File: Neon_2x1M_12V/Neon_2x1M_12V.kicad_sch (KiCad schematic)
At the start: 48 parts, among them J1 Conn_01x16_Pin, J2 Barrel_Jack_MountingPin, J3 Conn_01x16_Pin, J4 Barrel_Jack_MountingPin, J5 Barrel_Jack_MountingPin, J6 Conn_01x03_Pin, Q1 IRLML2502TRPBF, Q2 IRLML2502TRPBF, Q3 BSS138, Q4 BSS138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

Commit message: update BOM only 1k resistor is needed
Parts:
- Q3, Q4, Q5: value BSS138 -> Si2302DS; link https://makerselectronics.com/product/smd-mosfet-transistor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 -> https://uge-one.com/product/si2302ds-sot23-general-purpose-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
- R1: value 2.2k Ohm -> 1k Ohm
- R13: value 660 Ohm -> 680 Ohm
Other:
- note added: "BLUE LED, Vf=3V: V accross resistor = 3.3 - 3 = 0.3V I = V/R = 0.3/1000 = 0.3mAmp"
- note added: "for each LED (color): R = (Vsource - Vf) / I_Led p_R = (Vsource - Vf) * I_Led Red (Vf = 2.1 V) V_r = 12 − 2.1 = 9.9 V R = 9.9 / 0.015 = 660 Ω use standard 680 Ω I = 9.9 / 680 Ω = 14.5 mAmp P_R = 9.9 * 0.0145 = 0.14355 W (1/4 W resistor fine) Green (Vf = 2.8 V) V_r = 12 − 2.8 = 9.2 V R = 9.2 / 0.015 = 613.33 Ω use standard 600Ω I = 9.2 / 600 Ω = 15.3 mAmp P_R = 9.2 * 0.0153 = 0.14076 W Blue (Vf = 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"
- note removed: "BLUE LED, Vf=3V: V accross resistor = 3.3 - 3 = 0.3V I = V/R = 0.3/2200 = 0.59mAmp"
- note removed: "for each LED (color): R = (Vsource - Vf) / I_Led p_R = (Vsource - Vf) * I_Led Per LED current = 12 mA / 3 LEDs = 4.0 mA each. Red (Vf = 2.1 V) V_r = 12 − 2.1 = 9.9 V R = 9.9 / 0.015 = 660 Ω use standard 680 Ω I = 9.9 / 680 Ω = 14.5 mAmp P_R = 9.9 * 0.0145 = 0.14355 W (1/4 W resistor fine) Green (Vf = 2.8 V) V_r = 12 − 2.8 = 9.2 V R = 9.2 / 0.015 = 613.33 Ω use standard 600Ω I = 9.2 / 600 Ω = 15.3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"
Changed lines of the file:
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@@
 		)
 	)
-	(text "for each LED (color):\nR = (Vsource - Vf) / I_Led\np_R = (Vsource - Vf) * I_Led\n\nPer LED current = 12 mA / 3 LEDs = 4.0 mA each.\n\nRed (Vf = 2.1 V)\nV_r = 12 − 2.1 = 9.9 V\nR = 9.9 / 0.015 = 660 Ω \nuse standard 680 Ω\nI = 9.9 / 680 Ω = 14.5 mAmp\nP_R = 9.9 * 0.0145 = 0.14355 W (1/4 W resistor fine)\n\nGreen (Vf = 2.8 V)\nV_r = 12 − 2.8 = 9.2 V\nR = 9.2 / 0.015 = 613.33 Ω \nuse standard  600Ω\nI = 9.2 / 600 Ω = 15.3 mAmp\nP_R = 9.2 * 0.0153 = 0.14076 W\n\nBlue (Vf = 3.2 V)\nsame as green "
+	(text "for each LED (color):\nR = (Vsource - Vf) / I_Led\np_R = (Vsource - Vf) * I_Led\n\nRed (Vf = 2.1 V)\nV_r = 12 − 2.1 = 9.9 V\nR = 9.9 / 0.015 = 660 Ω \nuse standard 680 Ω\nI = 9.9 / 680 Ω = 14.5 mAmp\nP_R = 9.9 * 0.0145 = 0.14355 W (1/4 W resistor fine)\n\nGreen (Vf = 2.8 V)\nV_r = 12 − 2.8 = 9.2 V\nR = 9.2 / 0.015 = 613.33 Ω \nuse standard  600Ω\nI = 9.2 / 600 Ω = 15.3 mAmp\nP_R = 9.2 * 0.0153 = 0.14076 W\n\nBlue (Vf = 2.8 V)\nsame as green "
 		(exclude_from_sim no)
 		(at 96.012 156.464 0)
@@
 		)
 	)
-	(text "BLUE LED, Vf=3V:\nV accross resistor = 3.3 - 3 = 0.3V\nI = V/R = 0.3/2200 = 0.59mAmp"
+	(text "BLUE LED, Vf=3V:\nV accross resistor = 3.3 - 3 = 0.3V\nI = V/R = 0.3/1000 = 0.3mAmp"
 		(exclude_from_sim no)
 		(at 185.928 105.664 0)
@@
 			)
 		)
-		(property "Value" "660 Ohm"
+		(property "Value" "680 Ohm"
 			(at 142.24 82.55 90)
 			(effects
@@
 			)
 		)
-		(property "Value" "BSS138"
+		(property "Value" "Si2302DS"
 			(at 114.808 119.634 0)
 			(effects
@@
 			)
 		)
-		(property "Datasheet" "https://www.onsemi.com/pub/Collateral/BSS138-D.PDF"
+		(property "Datasheet" "https://www.vishay.com/docs/68645/si2302cds.pdf"
 			(at 114.3 121.92 0)
 			(effects
@@
 			)
 		)
-		(property "Description" "50V Vds, 0.22A Id, N-Channel MOSFET, SOT-23"
+		(property "Description" ""
 			(at 109.22 118.11 0)
 			(effects
@@
 			)
 		)
-		(property "link" "https://makerselectronics.com/product/smd-mosfet-transistor-bss138-j1-50v-220ma-3-5%CF%8910v220ma-360mw-n-channel-sot-23/?srsltid=AfmBOorKPkIxsAwv-3Onwyym6kfiJ7AE8Pv9g0Pld8GAUTAgILHxbmr_"
+		(property "link" "https://uge-one.com/product/si2302ds-sot23-general-purpose-n-channel-mosfet-smd-transistor-sot-23/"
 			(at 109.22 118.11 0)
 			(effects
@@
 			)
 		)
-		(property "Value" "BSS138"
+		(property "Value" "Si2302DS"
 			(at 114.808 80.264 0)
 			(effects
@@
 			)
 		)
-		(property "Datasheet" "https://www.onsemi.com/pub/Collateral/BSS138-D.PDF"
+		(property "Datasheet" "https://www.vishay.com/docs/68645/si2302cds.pdf"
 			(at 114.3 82.55 0)
 			(effects
@@
 			)
 		)
-		(property "Description" "50V Vds, 0.22A Id, N-Channel MOSFET, SOT-23"
+		(property "Description" ""
 			(at 109.22 78.74 0)
 			(effects
@@
 			)
 		)
-		(property "link" "https://makerselectronics.com/product/smd-mosfet-transistor-bss138-j1-50v-220ma-3-5%CF%8910v220ma-360mw-n-channel-sot-23/?srsltid=AfmBOorKPkIxsAwv-3Onwyym6kfiJ7AE8Pv9g0Pld8GAUTAgILHxbmr_"
+		(property "link" "https://uge-one.com/product/si2302ds-sot23-general-purpose-n-channel-mosfet-smd-transistor-sot-23/"
 			(at 109.22 78.74 0)
 			(effects
@@
 			)
 		)
-		(property "Value" "2.2k Ohm"
+		(property "Value" "1k Ohm"
 			(at 195.58 71.1199 0)
 			(effects
@@
 			)
 		)
-		(property "Value" "BSS138"
+		(property "Value" "Si2302DS"
 			(at 114.808 101.854 0)
 			(effects
@@
 			)
 		)
-		(property "Datasheet" "https://www.onsemi.com/pub/Collateral/BSS138-D.PDF"
+		(property "Datasheet" "https://www.vishay.com/docs/68645/si2302cds.pdf"
 			(at 114.3 104.14 0)
 			(effects
@@
 			)
 		)
-		(property "Description" "50V Vds, 0.22A Id, N-Channel MOSFET, SOT-23"
+		(property "Description" ""
 			(at 109.22 100.33 0)
 			(effects
@@
 			)
 		)
-		(property "link" "https://makerselectronics.com/product/smd-mosfet-transistor-bss138-j1-50v-220ma-3-5%CF%8910v220ma-360mw-n-channel-sot-23/?srsltid=AfmBOorKPkIxsAwv-3Onwyym6kfiJ7AE8Pv9g0Pld8GAUTAgILHxbmr_"
+		(property "link" "https://uge-one.com/product/si2302ds-sot23-general-purpose-n-channel-mosfet-smd-transistor-sot-23/"
 			(at 109.22 100.33 0)
 			(effects

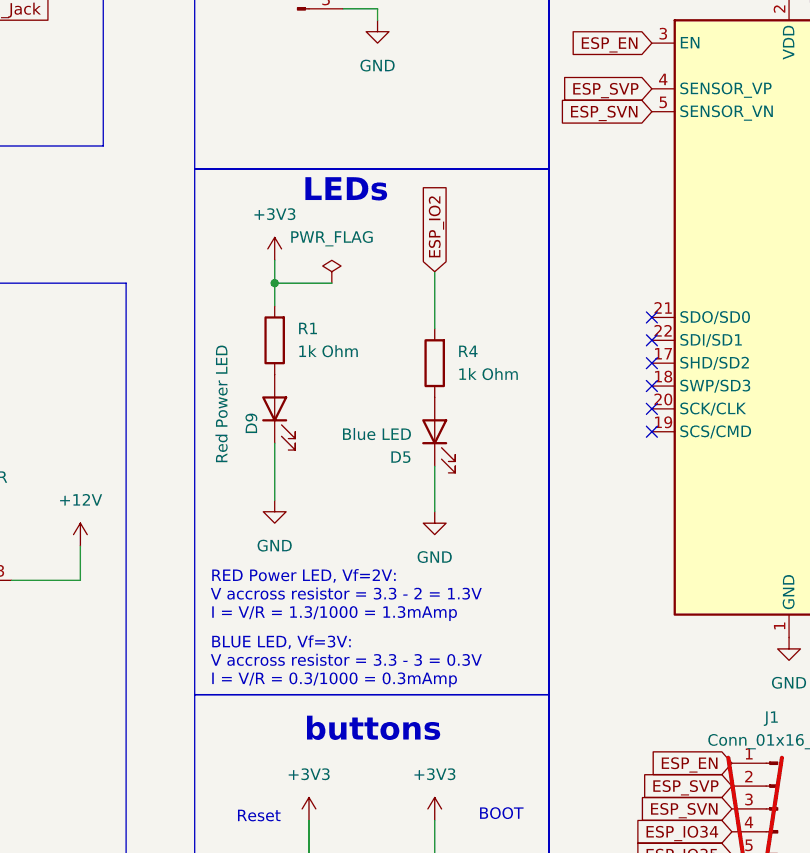
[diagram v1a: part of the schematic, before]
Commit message: removed blue led and replaced it with red one and also updated their current imiting resistor
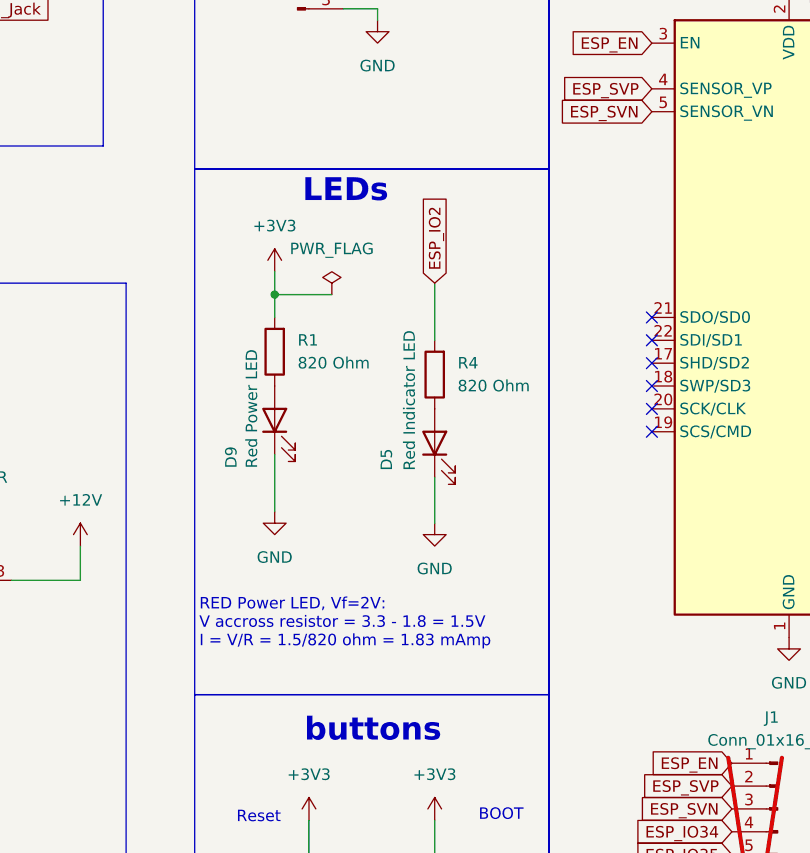
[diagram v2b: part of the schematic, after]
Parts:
- D5: value Blue LED -> Red Indicator LED
- R1: value 1k Ohm -> 820 Ohm; link https://makerselectronics.com/product/chip-resistor-smd-2-2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 -> https://uge-one.com/product/smd-chip-resistor-size-1206-820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
- R4: value 1k Ohm -> 820 Ohm; link https://makerselectronics.com/product/chip-resistor-smd-1k%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 -> https://uge-one.com/product/smd-chip-resistor-size-1206-820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
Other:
- note added: "RED Power LED, Vf=2V: V accross resistor = 3.3 - 1.8 = 1.5V I = V/R = 1.5/820 ohm = 1.83 mAmp"
- note removed: "BLUE LED, Vf=3V: V accross resistor = 3.3 - 3 = 0.3V I = V/R = 0.3/1000 = 0.3mAmp"
- note removed: "RED Power LED, Vf=2V: V accross resistor = 3.3 - 2 = 1.3V I = V/R = 1.3/1000 = 1.3mAmp"
- moved on the sheet: D5, D9, R1, R4
